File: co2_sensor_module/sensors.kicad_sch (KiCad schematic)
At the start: 6 parts, among them U5 MS5611-01BA, U6 SHT4x, U7 STC31-C

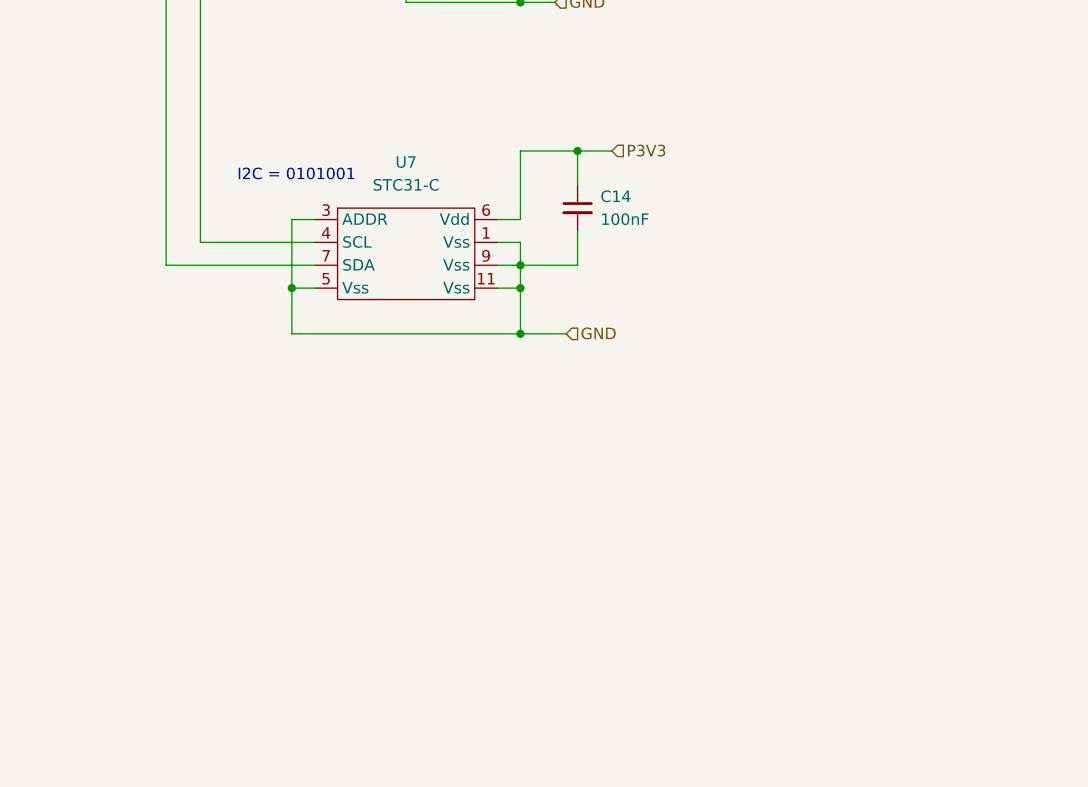
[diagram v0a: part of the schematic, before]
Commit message: added wip hub + o2 sensor
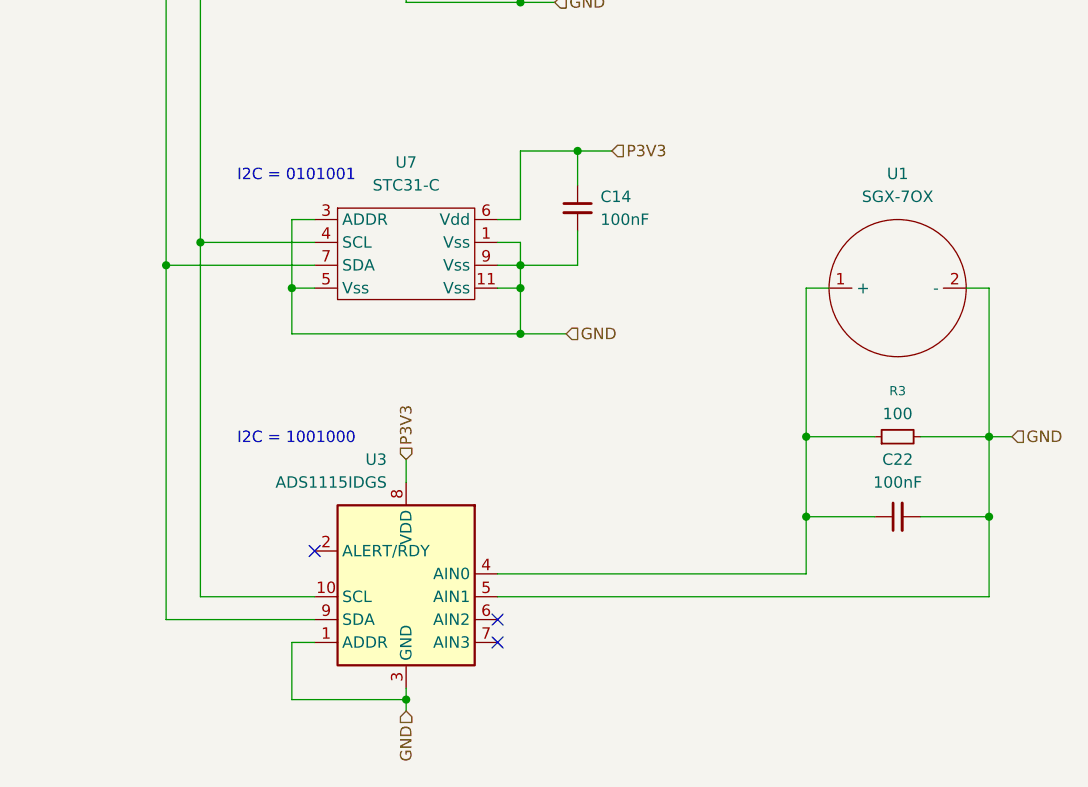
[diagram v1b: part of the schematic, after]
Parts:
- added C22: 100nF, Capacitor_SMD:C_0402_1005Metric, symbol Device:C_Small
- added R3: 100, Resistor_SMD:R_0201_0603Metric, symbol Device:R_Small
- added U1: SGX-7OX, CustomFootprints:SGX-7OX, symbol CustomSymbols:SGX-7OX
- added U3: ADS1115IDGS, Package_SO:TSSOP-10_3x3mm_P0.5mm, symbol Analog_ADC:ADS1115IDGS
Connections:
- net GND: now also C22.2, R3.2, U1.2 (-), U3.1 (ADDR), U3.3 (GND), U3.5 (AIN1)
- net I2C_SCL: now also U3.10 (SCL)
- net I2C_SDA: now also U3.9 (SDA)
- net P3V3: now also U3.8 (VDD)
- new net: C22.1, R3.1, U1.1 (+), U3.4 (AIN0)
- no-connect marks 1 -> 4
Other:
- note added: "I2C = 1001000"

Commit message: more routing
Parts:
- added C23: 100nF, Capacitor_SMD:C_0402_1005Metric, symbol Device:C_Small
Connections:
- net GND: now also C23.2
- net P3V3: now also C23.1
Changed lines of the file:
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@@
+	)
+	(junction
+		(at 106.68 147.32)
+		(diameter 0)
+		(color 0 0 0 0)
 	)
 	(junction
@@
 	(wire
 		(pts
-			(xy 106.68 146.05) (xy 106.68 148.59)
+			(xy 106.68 146.05) (xy 106.68 147.32)
 		)
 		(stroke
@@
 	(wire
 		(pts
+			(xy 115.57 147.32) (xy 118.11 147.32)
+		)
+		(stroke
+			(width 0)
+			(type default)
+		)
+	)
+	(wire
+		(pts
 			(xy 83.82 161.29) (xy 83.82 121.92)
 		)
@@
 	(wire
 		(pts
+			(xy 106.68 147.32) (xy 106.68 148.59)
+		)
+		(stroke
+			(width 0)
+			(type default)
+		)
+	)
+	(wire
+		(pts
 			(xy 171.45 127) (xy 171.45 143.51)
 		)
@@
 		(pts
 			(xy 96.52 46.99) (xy 80.01 46.99)
+		)
+		(stroke
+			(width 0)
+			(type default)
+		)
+	)
+	(wire
+		(pts
+			(xy 106.68 147.32) (xy 110.49 147.32)
 		)
 		(stroke
@@
 		(shape input)
 		(at 129.54 111.76 0)
+		(effects
+			(font
+				(size 1.27 1.27)
+			)
+			(justify left)
+		)
+	)
+	(hierarchical_label "GND"
+		(shape input)
+		(at 118.11 147.32 0)
 		(effects
 			(font
@@
 					(unit 1)
 				)
+			)
+		)
+	)
+	(symbol
+		(lib_id "Device:C_Small")
+		(at 113.03 147.32 90)
+		(unit 1)
+		(body_style 1)
+		(exclude_from_sim no)
+		(in_bom yes)
+		(on_board yes)
+		(in_pos_files yes)
+		(dnp no)
+		(fields_autoplaced yes)
+		(property "Reference" "C23"
+			(at 113.0363 140.97 90)
+			(show_name no)
+			(do_not_autoplace no)
+			(effects
+				(font
+					(size 1.27 1.27)
+				)
+			)
+		)
+		(property "Value" "100nF"
+			(at 113.0363 143.51 90)
+			(show_name no)
+			(do_not_autoplace no)
+			(effects
+				(font
+					(size 1.27 1.27)
+				)
+			)
+		)
+		(property "Footprint" "Capacitor_SMD:C_0402_1005Metric"
+			(at 113.03 147.32 0)
+			(hide yes)
+			(show_name no)
+			(do_not_autoplace no)
+			(effects
+				(font
+					(size 1.27 1.27)
+				)
+			)
+		)
+		(property "Datasheet" ""
+			(at 113.03 147.32 0)
+			(hide yes)
+			(show_name no)
+			(do_not_autoplace no)
+			(effects
+				(font
+					(size 1.27 1.27)
+				)
+			)
+		)
+		(property "Description" "Unpolarized capacitor, small symbol"
+			(at 113.03 147.32 0)
+			(hide yes)
+			(show_name no)
+			(do_not_autoplace no)
+			(effects
+				(font
+					(size 1.27 1.27)
+				)
+			)
+		)
+		(property "LCSC" "C1525"
+			(at 113.03 147.32 0)
+			(hide yes)
+			(show_name no)
+			(do_not_autoplace no)
+			(effects
+				(font
+					(size 1.27 1.27)
+				)
+			)
+		)
+		(pin "1"
+		)
+		(pin "2"
+		)
+		(instances
+			(project "co2_sensor_module"
+				(path "/58639344-3050-41c9-a876-6afa82650aa6/b6285f15-3a4b-493b-9028-ba58592b09d4"
+					(reference "C23")
+					(unit 1)
+				)

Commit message: mostly done with sensor module
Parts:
- R3: footprint Resistor_SMD:R_0201_0603Metric -> Resistor_SMD:R_0603_1608Metric
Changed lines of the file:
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@@
 			)
 		)
-		(property "Footprint" "Resistor_SMD:R_0201_0603Metric"
+		(property "Footprint" "Resistor_SMD:R_0603_1608Metric"
 			(at 161.29 143.51 0)
 			(hide yes)

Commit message: (mostly) finalized sensing units + progress on surface hub
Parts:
- added C24: 100nF, Capacitor_SMD:C_0402_1005Metric, symbol Device:C_Small
- added C25: 1uF, Capacitor_SMD:C_0603_1608Metric, symbol Device:C_Small
- added U11: SGP41-D-R4, CustomFootprints:XDCR_SGP41-D-R4, symbol CustomSymbols:SGP41-D-R4
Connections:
- net GND: now also C24.2, C25.2, U11.2 (VSS), U11.4 (N/A)
- net I2C_SCL: now also U11.3 (SDA)
- net I2C_SDA: now also U11.6 (SCL)
- net P3V3: now also C24.1, C25.1, U11.1 (VDD), U11.5 (VDDH)
- no-connect marks 4 -> 5
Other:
- note added: "I2C = 1011001"
- moved on the sheet: C14, C22, C23, R3, U1, U3, U7
